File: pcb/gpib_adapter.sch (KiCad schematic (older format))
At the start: 33 parts, among them CON1 AVR-ISP-6, J1 HEADER_5x2, P2 USB, P5 GPIB, U1 SN75160, U2 SN75161, U3 FT230XQ, U4 AT90CAN128-A

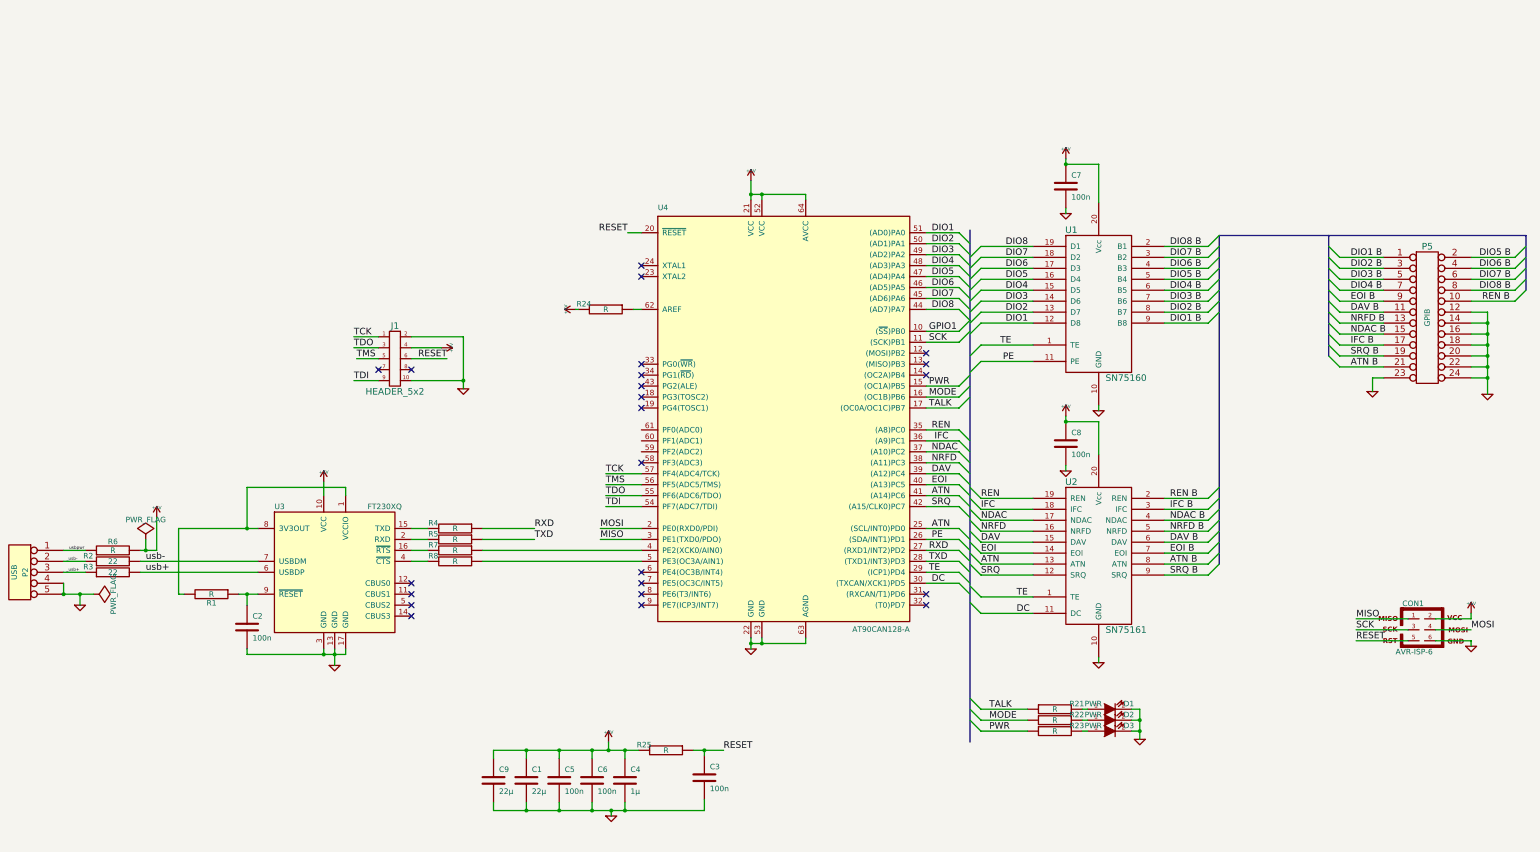
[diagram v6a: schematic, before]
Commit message: change microcontroller to pic18F to save costs
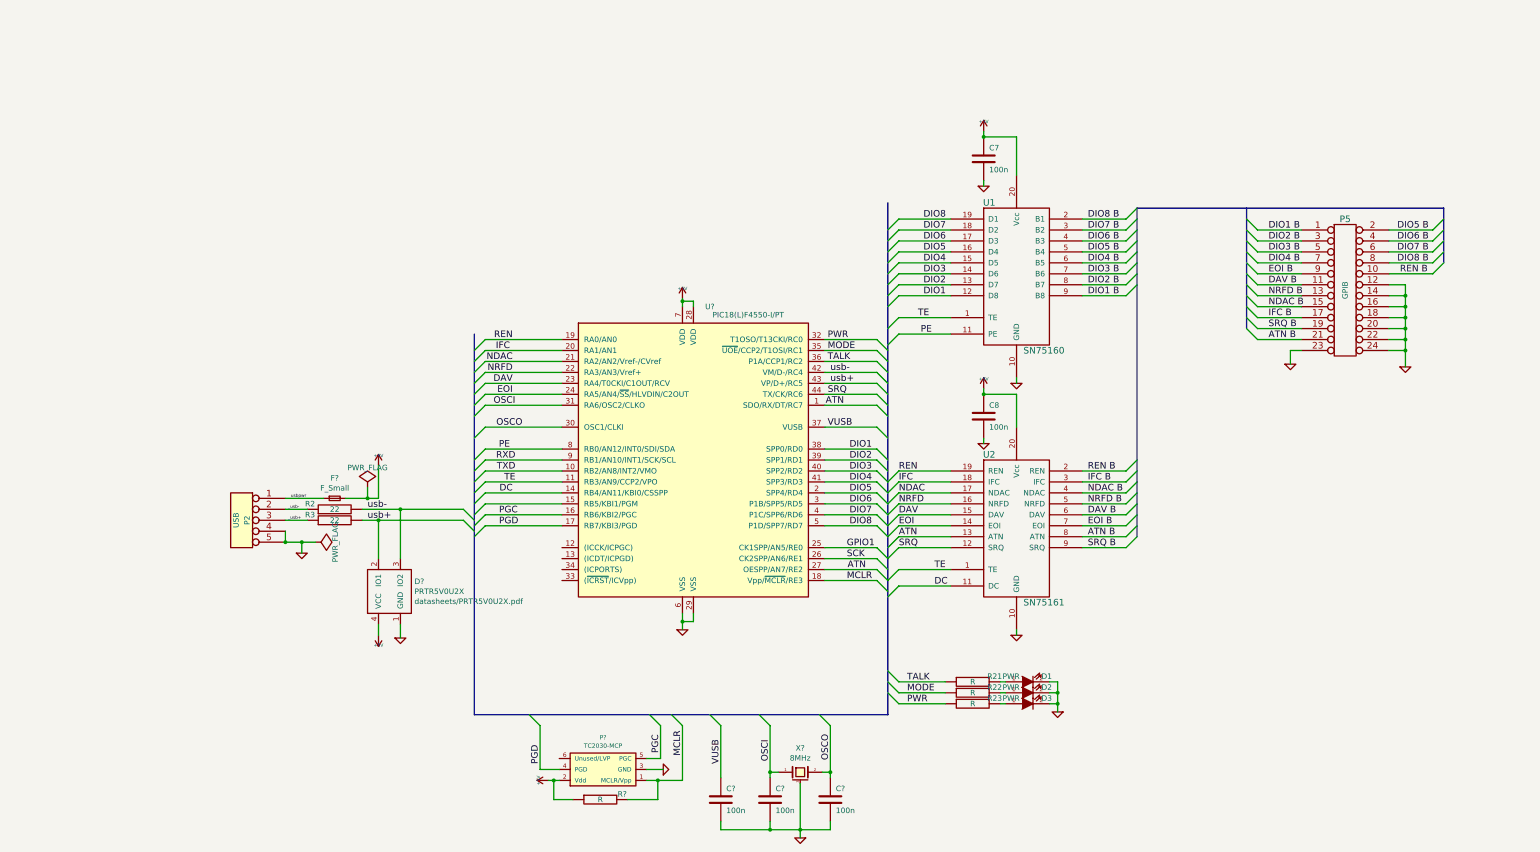
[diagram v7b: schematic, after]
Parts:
- removed C1, C9: 22µ, Capacitors_SMD:c_elec_5x5.3, symbol C-RESCUE-gpib_adapter
- removed C2, C3, C5, C6: 100n, Capacitors_SMD:C_0805, symbol C-RESCUE-gpib_adapter
- removed C4: 1µ, Capacitors_SMD:C_0805, symbol C-RESCUE-gpib_adapter
- removed CON1: AVR-ISP-6, w_pin_strip:pin_socket_3x2, symbol AVR-ISP-6
- removed J1: HEADER_5x2, w_pin_strip:pin_strip_5x2, symbol HEADER_5x2
- removed R1, R24, R25, R4, R5, R7, R8: R, Resistors_SMD:R_0805, symbol R-RESCUE-gpib_adapter
- removed R6: R, Resistors_SMD:R_1210, symbol R-RESCUE-gpib_adapter
- removed U3: FT230XQ, Housings_DFN_QFN:QFN-16-1EP_4x4mm_Pitch0.65mm, symbol FT230XQ
- removed U4: AT90CAN128-A, Housings_QFP:LQFP-64_14x14mm_Pitch0.8mm, symbol AT90CAN128-A
- added C? (x3): 100n, Capacitors_SMD:C_0805, symbol C-RESCUE-gpib_adapter
- added D?: PRTR5V0U2X, symbol PRTR5V0U2X
- added F?: F_Small, symbol F_Small
- added P?: TC2030-MCP, symbol TC2030-MCP
- added R?: R, Resistors_SMD:R_0805, symbol R-RESCUE-gpib_adapter
- added U?: PIC18(L)F4550-I/PT, TQFP44, symbol PIC18(L)F4550-I/PT
- added X?: 8MHz, symbol CRYSTAL_SMD
- P5: Digikey (none) -> 1024RFA-ND
- U1: Digikey (none) -> 296-14950-1-ND
- U2: Digikey (none) -> 296-6846-5-ND
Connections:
- net +5V: now also D?.4 (VCC), F?.2, P?.2 (Vdd), R?.1, U?.28 (VDD), U?.7 (VDD)
- net ATN: now also U?.1 (SDO/RX/DT/RC7), U?.27 (OESPP/AN7/RE2)
- net DAV: now also U?.23 (RA4/T0CKI/C1OUT/RCV)
- net DC: now also U?.14 (RB4/AN11/KBI0/CSSPP)
- net DIO1: now also U?.38 (SPP0/RD0)
- net DIO2: now also U?.39 (SPP1/RD1)
- net DIO3: now also U?.40 (SPP2/RD2)
- net DIO4: now also U?.41 (SPP3/RD3)
- net DIO5: now also U?.2 (SPP4/RD4)
- net DIO6: now also U?.3 (P1B/SPP5/RD5)
- net DIO7: now also U?.4 (P1C/SPP6/RD6)
- net DIO8: now also U?.5 (P1D/SPP7/RD7)
- net EOI: now also U?.24 (RA5/AN4/~SS~/HLVDIN/C2OUT)
- net GND: now also C?.2, C?.2, C?.2, D?.1 (GND), P?.3 (GND), U?.29 (VSS), U?.6 (VSS), X?.3 (case)
- net GPIO1: now also U?.25 (CK1SPP/AN5/RE0)
- net IFC: now also U?.20 (RA1/AN1)
- net MODE: now also U?.35 (~UOE~/CCP2/T1OSI/RC1)
- net NDAC: now also U?.21 (RA2/AN2/Vref-/CVref)
- net NRFD: now also U?.22 (RA3/AN3/Vref+)
- net PE: now also U?.8 (RB0/AN12/INT0/SDI/SDA)
- net PWR: now also U?.32 (T1OSO/T13CKI/RC0)
- net REN: now also U?.19 (RA0/AN0)
- net RXD: now also U?.9 (RB1/AN10/INT1/SCK/SCL)
- net SCK: now also U?.26 (CK2SPP/AN6/RE1)
- net SRQ: now also U?.44 (TX/CK/RC6)
- net TALK: now also U?.36 (P1A/CCP1/RC2)
- net TE: now also U?.11 (RB3/AN9/CCP2/VPO)
- net TXD: now also U?.10 (RB2/AN8/INT2/VMO)
- net usb+: now also D?.2 (IO1), U?.43 (VP/D+/RC5)
- net usb-: now also D?.3 (IO2), U?.42 (VM/D-/RC4)
- net usbpwr: now also F?.1
- new net MCLR: P?.1 (MCLR/Vpp), R?.2, U?.18 (Vpp/~MCLR~/RE3)
- new net OSCI: C?.1, U?.31 (RA6/OSC2/CLKO), X?.1
- new net OSCO: C?.1, U?.30 (OSC1/CLKI), X?.2
- new net PGC: P?.5 (PGC), U?.16 (RB6/KBI2/PGC)
- new net PGD: P?.4 (PGD), U?.17 (RB7/KBI3/PGD)
- new net VUSB: C?.1, U?.37 (VUSB)
- no-connect marks 23 -> 0
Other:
- moved on the sheet: C7, C8, D1, D2, D3, P2, P5, R2, R21, R22, R23, R3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

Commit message: add enclosure drawing
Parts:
- removed R21, R22, R23: R, Resistors_SMD:R_0805, symbol R-RESCUE-gpib_adapter
- added R4, R5, R6: 470, Resistors_SMD:R_0805, symbol R
- C1: renamed from C?; value 100n -> 1u; symbol C-RESCUE-gpib_adapter -> C
- C2, C3: renamed from C?; value 100n -> 18p; symbol C-RESCUE-gpib_adapter -> C
- C7, C8: symbol C-RESCUE-gpib_adapter -> C
- D1, D2, D3: footprint Capacitors_SMD:C_0805 -> LEDs:LED-5MM
- D4: renamed from D?; footprint (none) -> esd_protection:PRTR5V0U2X
- F1: renamed from F?; footprint (none) -> Resistors_SMD:R_1210
- P1: renamed from P?; footprint (none) -> tagconnect:TC2030-NL_SMALL
- P5: footprint w_pin_strip:pin_socket_12x2 -> gpib_conn_male:gpib_conn_male
- R2, R3: symbol R-RESCUE-gpib_adapter -> R
- U3: renamed from U?; footprint TQFP44 -> Housings_QFP:TQFP-44_10x10mm_Pitch0.8mm
- X1: renamed from X?; footprint (none) -> Crystals:Crystal_SMD_5032_4Pads
- gave numbers to parts that had none: 1
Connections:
- net MODE: now also R5.2
- net PWR: now also R6.2
- net TALK: now also R4.2
- net at D1.1 (A): now also R4.1
- net at D2.1 (A): now also R5.1
- net at D3.1 (A): now also R6.1
- net GPIO1: no longer names the net of U3.25 (CK1SPP/AN5/RE0)
- net RXD: no longer names the net of U3.9 (RB1/AN10/INT1/SCK/SCL)
- net SCK: no longer names the net of U3.26 (CK2SPP/AN6/RE1)
- net TXD: no longer names the net of U3.10 (RB2/AN8/INT2/VMO)
- no-connect marks 0 -> 10
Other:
- moved on the sheet: C7, C8
